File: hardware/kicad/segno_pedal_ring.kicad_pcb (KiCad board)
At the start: 2 copper layers, 80 x 80 mm, 19 parts, among them J1 Conn_01x04, J2 NEOPIXEL, J3 RINGPINS24, J4 RINGPINS16, U1 XIAO-RP2350, U2 74AHCT125N

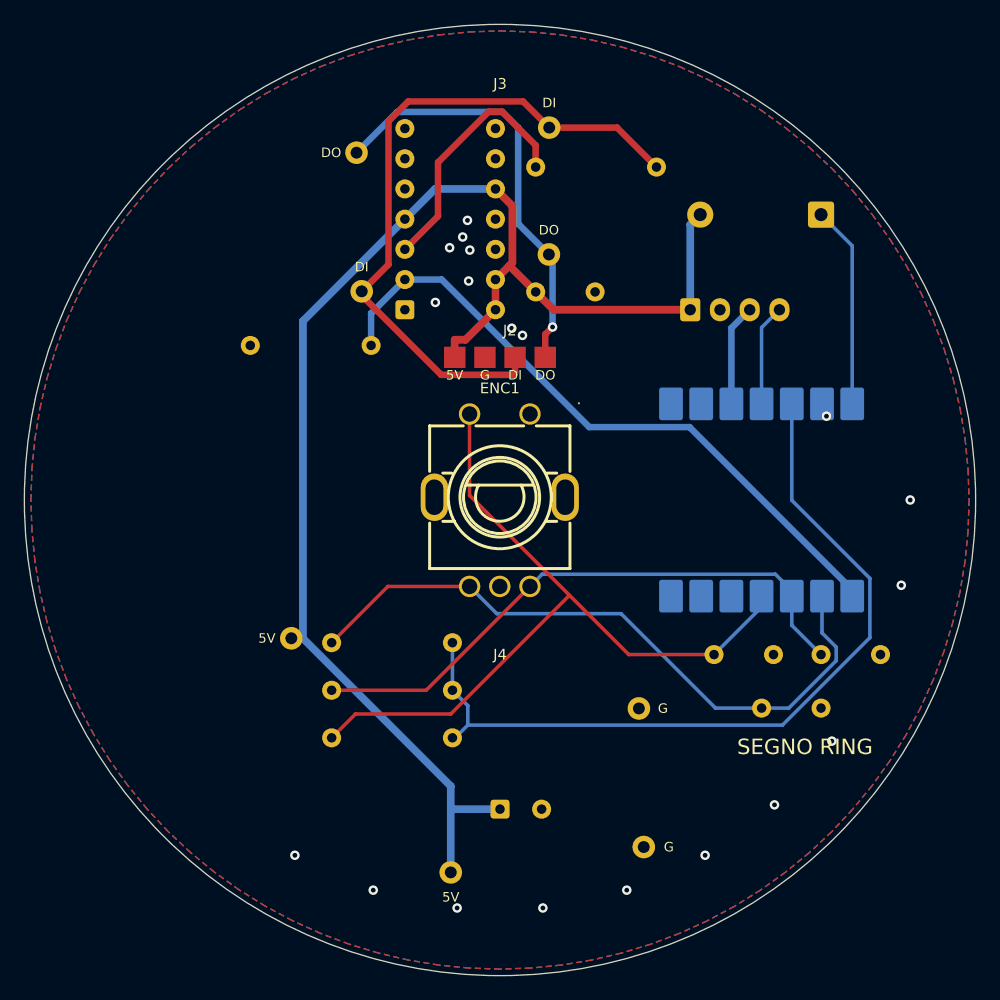
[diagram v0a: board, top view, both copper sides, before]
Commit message: feat(hardware): publish screen switching and board refinements
Add the hand-soldered two-layer screen-power board, aligned console connectors, ADC supply isolation, white ring carrier and reviewed manufacturing ZIPs. Integrate GPIO17 ownership with Weston startup and shutdown; retain assembled-system validation as the hardware gate.
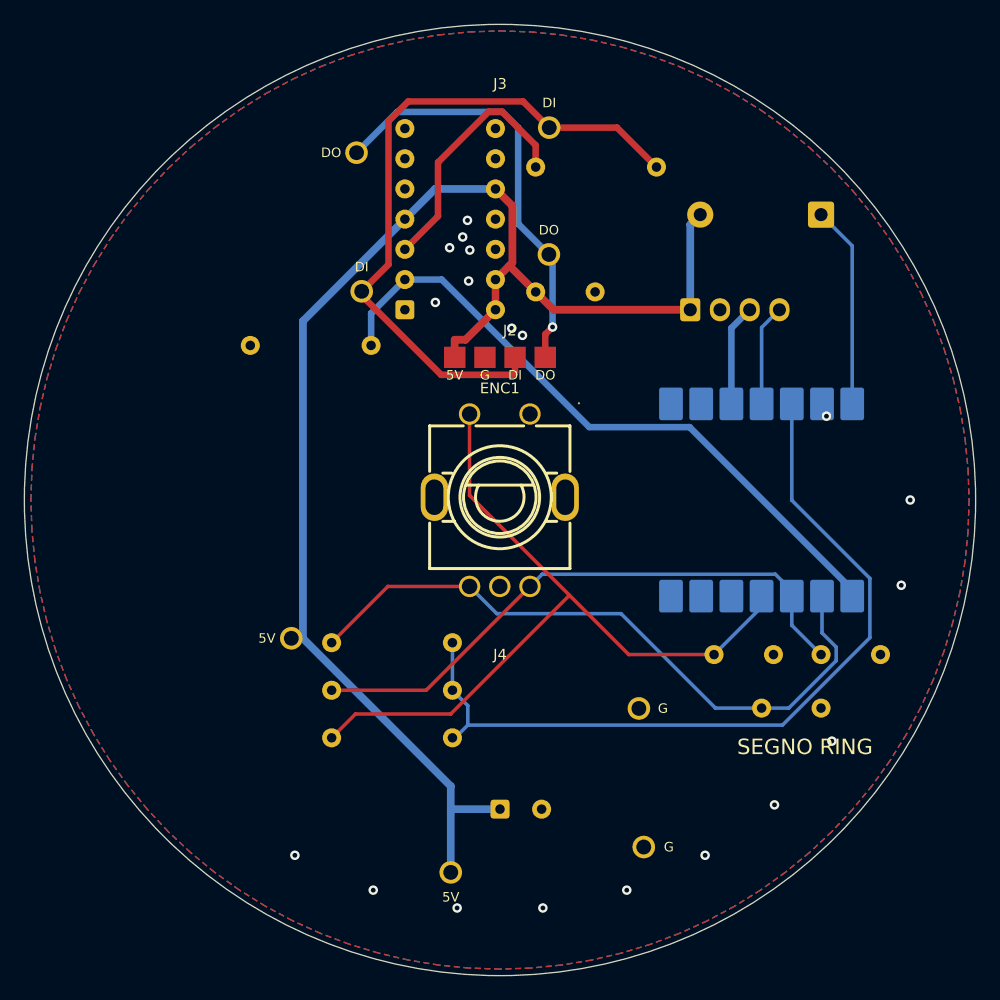
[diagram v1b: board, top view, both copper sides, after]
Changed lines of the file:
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@@
 			(layer "F.SilkS"
 				(type "Top Silk Screen")
-				(color "White")
+				(color "Black")
 			)
 			(layer "F.Paste"
@@
 			(layer "F.Mask"
 				(type "Top Solder Mask")
-				(color "Purple")
+				(color "White")
 				(thickness 0.01)
 			)
@@
 			(layer "B.Mask"
 				(type "Bottom Solder Mask")
-				(color "Purple")
+				(color "White")
 				(thickness 0.01)
 			)
@@
 			(layer "B.SilkS"
 				(type "Bottom Silk Screen")
-				(color "White")
+				(color "Black")
 			)
 			(copper_finish "None")
@@
 			(at 4.14 -31.318)
 			(size 1.9 1.9)
-			(drill 1)
+			(drill 1.25)
 			(layers "*.Cu" "*.Mask")
 			(remove_unused_layers no)
@@
 			(at -4.14 31.318)
 			(size 1.9 1.9)
-			(drill 1)
+			(drill 1.25)
 			(layers "*.Cu" "*.Mask")
 			(remove_unused_layers no)
@@
 			(at 12.09 29.185)
 			(size 1.9 1.9)
-			(drill 1)
+			(drill 1.25)
 			(layers "*.Cu" "*.Mask")
 			(remove_unused_layers no)
@@
 			(at -12.065 -29.21)
 			(size 1.9 1.9)
-			(drill 1)
+			(drill 1.25)
 			(layers "*.Cu" "*.Mask")
 			(remove_unused_layers no)
@@
 			(at -11.63 -17.55)
 			(size 1.9 1.9)
-			(drill 1)
+			(drill 1.25)
 			(layers "*.Cu" "*.Mask")
 			(remove_unused_layers no)
@@
 			(at -17.55 11.63)
 			(size 1.9 1.9)
-			(drill 1)
+			(drill 1.25)
 			(layers "*.Cu" "*.Mask")
 			(remove_unused_layers no)
@@
 			(at 11.68 17.53)
 			(size 1.9 1.9)
-			(drill 1)
+			(drill 1.25)
 			(layers "*.Cu" "*.Mask")
 			(remove_unused_layers no)
@@
 			(at 4.11 -20.65)
 			(size 1.9 1.9)
-			(drill 1)
+			(drill 1.25)
 			(layers "*.Cu" "*.Mask")
 			(remove_unused_layers no)
@@
 			(at 0 0)
 			(size 1.7 1.95)
-			(drill 0.95)
+			(drill 1.1)
 			(layers "*.Cu" "*.Mask")
 			(remove_unused_layers no)
@@
 			(at 2.5 0)
 			(size 1.7 1.95)
-			(drill 0.95)
+			(drill 1.1)
 			(layers "*.Cu" "*.Mask")
 			(remove_unused_layers no)
@@
 			(at 5 0)
 			(size 1.7 1.95)
-			(drill 0.95)
+			(drill 1.1)
 			(layers "*.Cu" "*.Mask")
 			(remove_unused_layers no)
@@
 			(at 7.5 0)
 			(size 1.7 1.95)
-			(drill 0.95)
+			(drill 1.1)
 			(layers "*.Cu" "*.Mask")
 			(remove_unused_layers no)

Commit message: fix(hardware): support full-white 40-pixel ring power
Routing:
- net +5V_LED: track 119.8 -> 142.5 mm
- net RING_DOUT: track 36.3 -> 38.1 mm
- net GND: vias 19 -> 20
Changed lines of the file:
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@@
+	)
+	(segment
+		(start 47 20)
+		(end 45 22)
+		(width 1.5)
+		(locked yes)
+		(layer "F.Cu")
+		(net "+5V_LED")
+	)
+	(segment
+		(start 52 20)
+		(end 47 20)
+		(width 1.5)
+		(locked yes)
+		(layer "F.Cu")
+		(net "+5V_LED")
 	)
 	(segment
@@
 	)
 	(segment
+		(start 45 22)
+		(end 32.189999 22)
+		(width 1.5)
+		(locked yes)
+		(layer "F.Cu")
+		(net "+5V_LED")
+	)
+	(segment
 		(start 36.79 16.29)
 		(end 35.62 17.46)
@@
 	)
 	(segment
+		(start 32.189999 22)
+		(end 32.189999 24)
+		(width 1.5)
+		(locked yes)
+		(layer "F.Cu")
+		(net "+5V_LED")
+	)
+	(segment
 		(start 35.62 9.84)
 		(end 30.54 9.84)
@@
 	)
 	(via
-		(at 37.8905 22.1547)
-		(size 0.8)
-		(drill 0.4)
-		(layers "F.Cu" "B.Cu")
-		(net "GND")
-	)
-	(via
 		(at 63.4562 28.9512)
 		(size 0.8)
@@
 	)
 	(via
+		(at 34.73 23.5)
+		(size 0.8)
+		(drill 0.4)
+		(layers "F.Cu" "B.Cu")
+		(locked yes)
+		(net "GND")
+	)
+	(via
 		(at 31.7633 14.7824)
 		(size 0.8)
@@
 	)
 	(via
+		(at 35.23 24)
+		(size 0.8)
+		(drill 0.4)
+		(layers "F.Cu" "B.Cu")
+		(locked yes)
+		(net "GND")
+	)
+	(via
 		(at 33.4633 14.9824)
 		(size 0.8)
@@
 	)
 	(via
-		(at 36.9905 21.5547)
-		(size 0.8)
-		(drill 0.4)
-		(layers "F.Cu" "B.Cu")
-		(net "GND")
-	)
-	(via
 		(at 33.2633 12.4824)
 		(size 0.8)
@@
 	)
 	(via
+		(at 34.23 24)
+		(size 0.8)
+		(drill 0.4)
+		(layers "F.Cu" "B.Cu")
+		(locked yes)
+		(net "GND")
+	)
+	(via
 		(at 46.6611 68.8114)
 		(size 0.8)
@@
 	)
 	(segment
-		(start 39.81 22.0642)
-		(end 39.81 24)
-		(width 0.55)
-		(layer "F.Cu")
-		(net "RING_DOUT")
-	)
-	(segment
-		(start 40.4206 21.4536)
-		(end 39.81 22.0642)
-		(width 0.55)
-		(layer "F.Cu")
-		(net "RING_DOUT")
-	)
-	(via
-		(at 40.4206 21.4536)
-		(size 0.8)
-		(drill 0.4)
-		(layers "F.Cu" "B.Cu")
-		(net "RING_DOUT")
-	)
-	(segment
-		(start 40.4206 15.6606)
-		(end 40.4206 21.4536)
-		(width 0.55)
-		(layer "B.Cu")
+		(start 39.81 24)
+		(end 39.81 24.9)
+		(width 0.3)
+		(layer "F.Cu")
+		(net "RING_DOUT")
+	)
+	(via
+		(at 39.81 24.9)
+		(size 0.8)
+		(drill 0.4)
+		(layers "F.Cu" "B.Cu")
 		(net "RING_DOUT")
 	)
@@
 	)
 	(segment
+		(start 40.4206 15.6606)
+		(end 40.4206 24.2894)
+		(width 0.3)
+		(layer "B.Cu")
+		(net "RING_DOUT")
+	)
+	(segment
 		(start 40.11 15.35)
 		(end 40.4206 15.6606)
@@
 		(layer "B.Cu")
 		(net "RING_DOUT")
+	)
+	(segment
+		(start 40.4206 24.2894)
+		(end 39.81 24.9)
+		(width 0.3)
+		(layer "B.Cu")
+		(net "RING_DOUT")

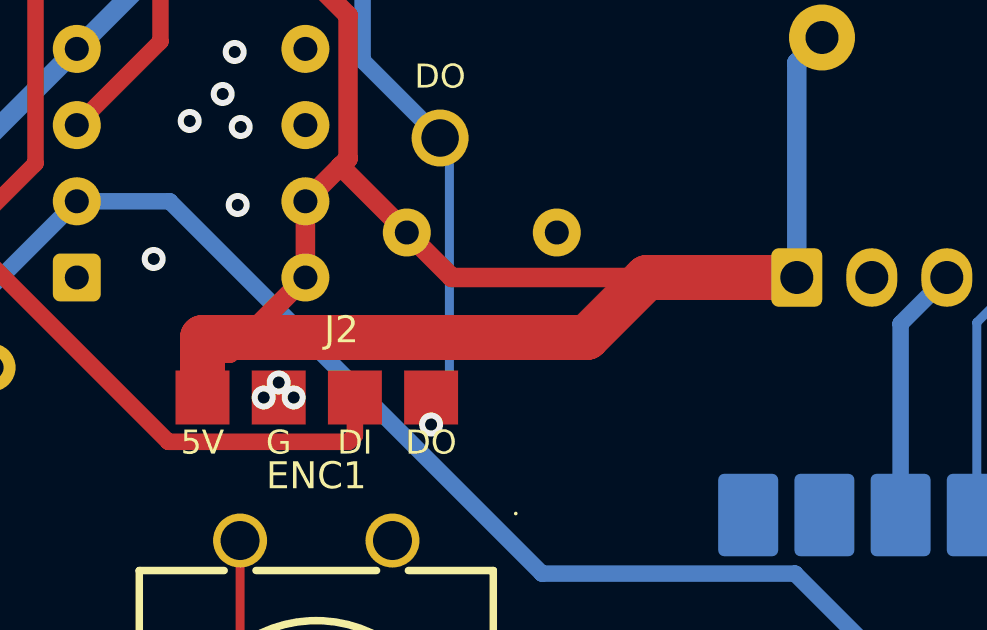
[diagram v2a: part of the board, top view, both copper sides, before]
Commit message: fix(hardware): strengthen screen gate drive and finish PCB copper
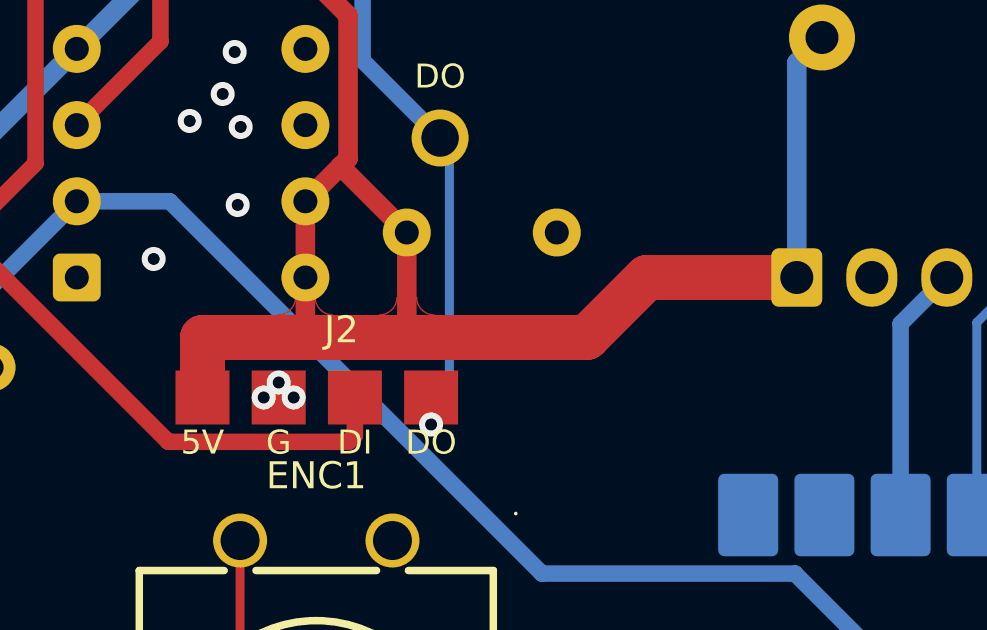
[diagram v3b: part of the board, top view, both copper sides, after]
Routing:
- net +5V_LED: track 142.5 -> 128.4 mm
- added copper zone on F.Cu, net +5V_LED
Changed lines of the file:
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@@
-	)
-	(segment
-		(start 52 20)
-		(end 40.5 20)
-		(width 0.65)
-		(layer "F.Cu")
-		(net "+5V_LED")
-	)
-	(segment
-		(start 40.5 20)
-		(end 39 18.5)
-		(width 0.65)
-		(layer "F.Cu")
-		(net "+5V_LED")
 	)
 	(segment
@@
 	)
 	(segment
+		(start 39 22)
+		(end 35.62 22)
+		(width 1.5)
+		(locked yes)
+		(layer "F.Cu")
+		(net "+5V_LED")
+	)
+	(segment
+		(start 39 18.5)
+		(end 39 22)
+		(width 0.65)
+		(locked yes)
+		(layer "F.Cu")
+		(net "+5V_LED")
+	)
+	(segment
+		(start 45 22)
+		(end 39 22)
+		(width 1.5)
+		(locked yes)
+		(layer "F.Cu")
+		(net "+5V_LED")
+	)
+	(segment
 		(start 35.62 17.46)
 		(end 35.62 20)
-		(width 0.65)
-		(layer "F.Cu")
-		(net "+5V_LED")
-	)
-	(segment
-		(start 32.19 24)
-		(end 32.19 22.5233)
 		(width 0.65)
 		(layer "F.Cu")
@@
 	)
 	(segment
-		(start 35.62 20)
-		(end 33.0967 22.5233)
-		(width 0.65)
-		(layer "F.Cu")
-		(net "+5V_LED")
-	)
-	(segment
-		(start 33.0967 22.5233)
-		(end 32.19 22.5233)
-		(width 0.65)
-		(layer "F.Cu")
-		(net "+5V_LED")
-	)
-	(segment
-		(start 45 22)
+		(start 35.62 22)
 		(end 32.189999 22)
 		(width 1.5)
@@
 		(end 35.62 17.46)
 		(width 0.65)
+		(layer "F.Cu")
+		(net "+5V_LED")
+	)
+	(segment
+		(start 35.62 20)
+		(end 35.62 22)
+		(width 0.65)
+		(locked yes)
 		(layer "F.Cu")
 		(net "+5V_LED")
@@
 			)
 		)
+	)
+	(zone
+		(net "+5V_LED")
+		(locked yes)
+		(layer "F.Cu")
+		(name "TAP_FILLET")
+		(hatch edge 0.5)
+		(priority 20)
+		(connect_pads yes
+			(clearance 0)
+		)
+		(min_thickness 0.05)
+		(fill yes
+			(thermal_gap 0.5)
+			(thermal_bridge_width 0.5)
+			(island_removal_mode 0)
+		)
+		(polygon
+			(pts
+				(xy 38.675 20.65) (xy 38.669867 20.728316) (xy 38.654555 20.805291) (xy 38.629328 20.87961) (xy 38.594615 20.95)
+				(xy 38.551012 21.015257) (xy 38.499264 21.074264) (xy 38.440257 21.126012) (xy 38.375 21.169615)
+				(xy 38.30461 21.204328) (xy 38.230291 21.229555) (xy 38.153316 21.244867) (xy 38.075 21.25) (xy 38.075 22)
+				(xy 39.925 22) (xy 39.925 21.25) (xy 39.846684 21.244867) (xy 39.769709 21.229555) (xy 39.69539 21.204328)
+				(xy 39.625 21.169615) (xy 39.559743 21.126012) (xy 39.500736 21.074264) (xy 39.448988 21.015257)
+				(xy 39.405385 20.95) (xy 39.370672 20.87961) (xy 39.345445 20.805291) (xy 39.330133 20.728316) (xy 39.325 20.65)
+			)
+		)
+	)
+	(zone
+		(net "+5V_LED")
+		(locked yes)
+		(layer "F.Cu")
+		(name "TAP_FILLET")
+		(hatch edge 0.5)
+		(priority 20)
+		(connect_pads yes
+			(clearance 0)
+		)
+		(min_thickness 0.05)
+		(fill yes
+			(thermal_gap 0.5)
+			(thermal_bridge_width 0.5)
+			(island_removal_mode 0)
+		)
+		(polygon
+			(pts
+				(xy 35.295 20.65) (xy 35.289867 20.728316) (xy 35.274555 20.805291) (xy 35.249328 20.87961) (xy 35.214615 20.95)
+				(xy 35.171012 21.015257) (xy 35.119264 21.074264) (xy 35.060257 21.126012) (xy 34.995 21.169615)
+				(xy 34.92461 21.204328) (xy 34.850291 21.229555) (xy 34.773316 21.244867) (xy 34.695 21.25) (xy 34.695 22)
+				(xy 36.545 22) (xy 36.545 21.25) (xy 36.466684 21.244867) (xy 36.389709 21.229555) (xy 36.31539 21.204328)
+				(xy 36.245 21.169615) (xy 36.179743 21.126012) (xy 36.120736 21.074264) (xy 36.068988 21.015257)
+				(xy 36.025385 20.95) (xy 35.990672 20.87961) (xy 35.965445 20.805291) (xy 35.950133 20.728316) (xy 35.945 20.65)
+			)
+		)

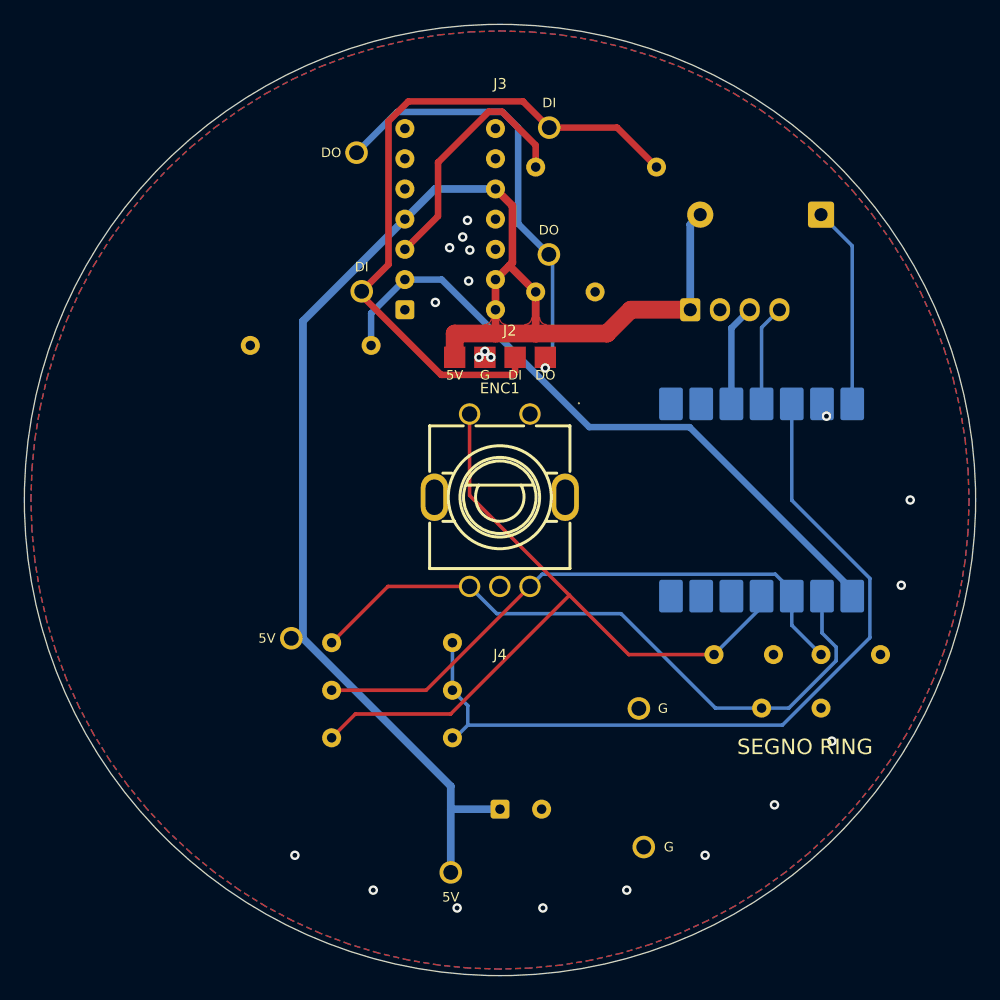
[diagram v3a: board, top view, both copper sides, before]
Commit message: fix(hardware): finish rounded routing across all three boards
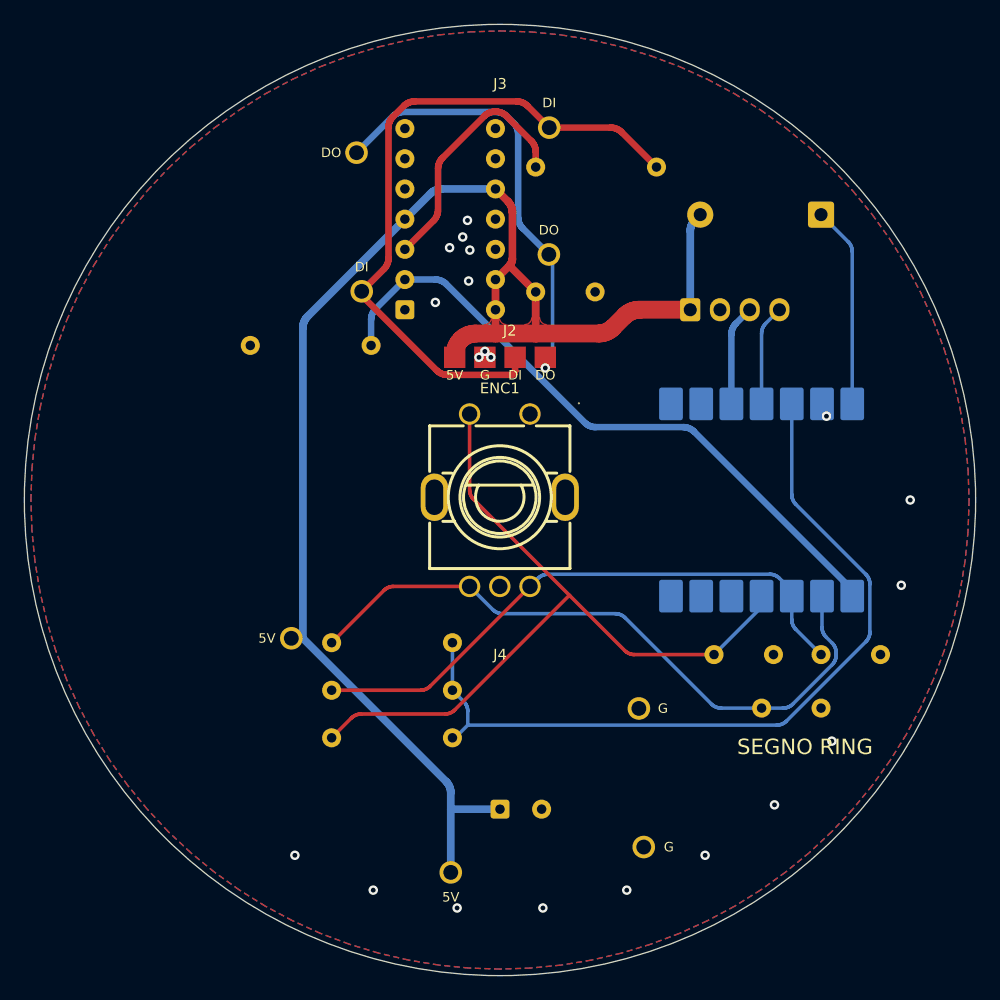
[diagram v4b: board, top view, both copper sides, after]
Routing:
- net +5V_LED: track 128.4 -> 127.1 mm
